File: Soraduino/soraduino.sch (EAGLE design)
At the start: 21 parts, among them IC1 ATMEGA168-AU, IC2 317EMP, IC3 317EMP

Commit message: 仮配線完了
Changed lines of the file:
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@@
 <wire x1="172.72" y1="0" x2="162.56" y2="0" width="0.1524" layer="91"/>
 <junction x="162.56" y="0"/>
-<junction x="172.72" y="0"/>
 <pinref part="IC4" gate="G$1" pin="DCPROG"/>
 <wire x1="137.16" y1="86.36" x2="162.56" y2="86.36" width="0.1524" layer="91"/>
 <junction x="162.56" y="86.36"/>
-<wire x1="172.72" y1="0" x2="254" y2="0" width="0.1524" layer="91"/>
 <pinref part="JAIRO-ANA" gate="G$1" pin="2"/>
 </segment>
@@
 </sheet>
 </sheets>
+<errors>
+</errors>
 </schematic>
 </drawing>

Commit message: back GPS 1
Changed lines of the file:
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@@
 <wire x1="172.72" y1="0" x2="162.56" y2="0" width="0.1524" layer="91"/>
 <junction x="162.56" y="0"/>
+<junction x="172.72" y="0"/>
 <pinref part="IC4" gate="G$1" pin="DCPROG"/>
 <wire x1="137.16" y1="86.36" x2="162.56" y2="86.36" width="0.1524" layer="91"/>
 <junction x="162.56" y="86.36"/>
+<wire x1="172.72" y1="0" x2="254" y2="0" width="0.1524" layer="91"/>
 <pinref part="JAIRO-ANA" gate="G$1" pin="2"/>
 </segment>
@@
 </sheet>
 </sheets>
-<errors>
-</errors>
 </schematic>
 </drawing>

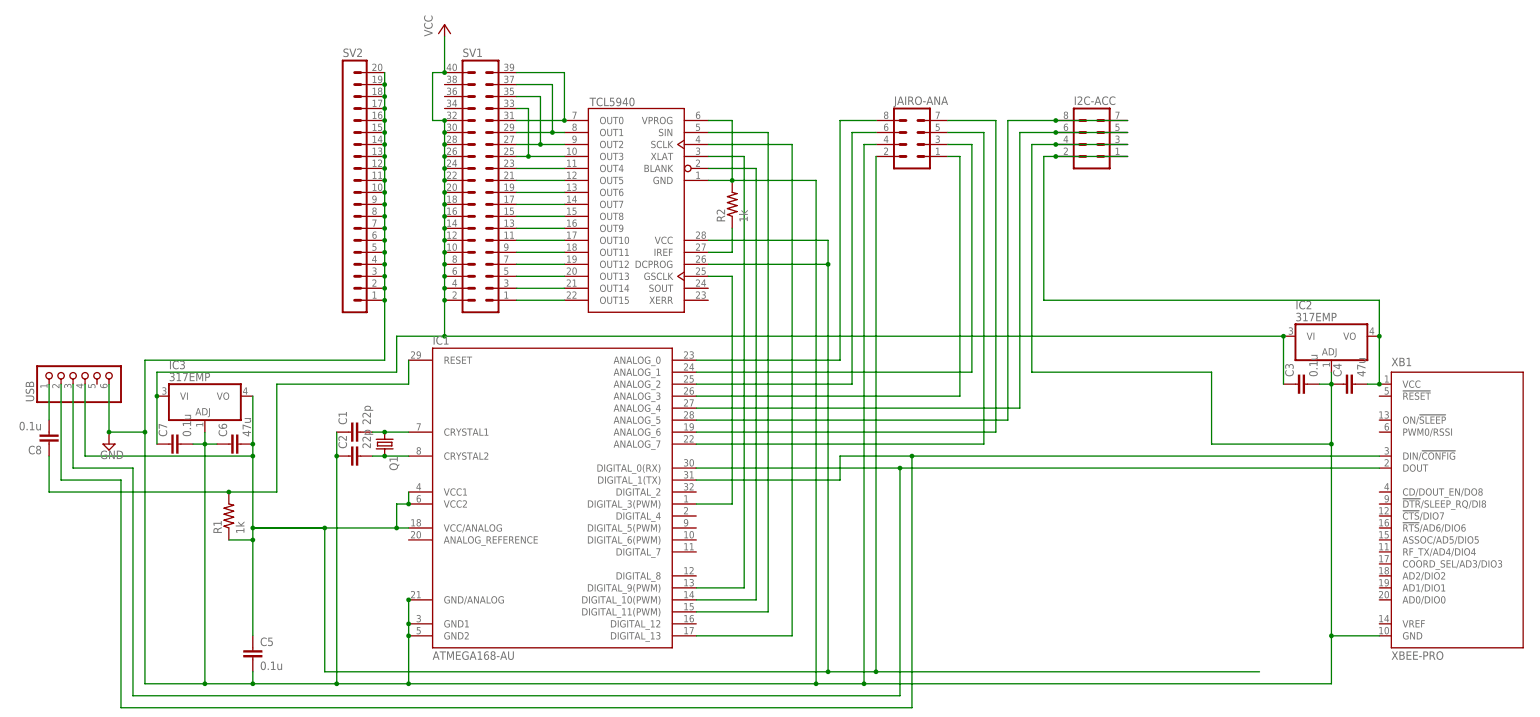
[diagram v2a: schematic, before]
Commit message: Revert "GPS、Digital出力を一旦削除"
This reverts commit f31cc228a309c3dd5619f128104a36497abb7aed.
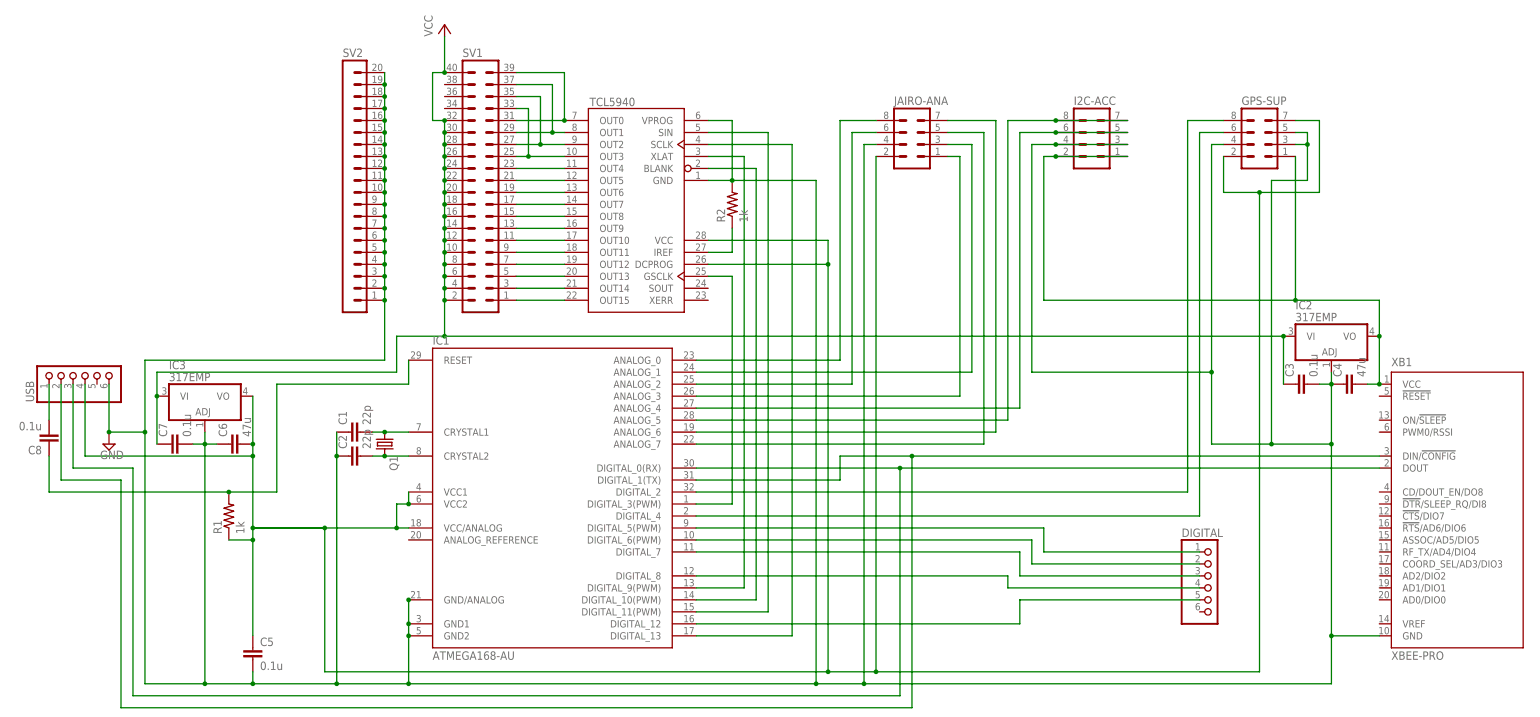
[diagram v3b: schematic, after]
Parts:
- added DIGITAL: (no value), pinhead:PINHD-1X6
- added GPS-SUP: (no value), con-lstb:MA04-2
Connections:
- new net N$36: GPS-SUP.8, IC1.DIGITAL_2
- new net N$37: GPS-SUP.6, IC1.DIGITAL_4
- new net N$39: DIGITAL.1, IC1.DIGITAL_5(PWM)
- new net N$40: DIGITAL.2, IC1.DIGITAL_6(PWM)
- new net N$41: DIGITAL.3, IC1.DIGITAL_7
- new net N$42: DIGITAL.4, IC1.DIGITAL_8
- new net N$47: DIGITAL.5, IC1.DIGITAL_12
- net GND: now also GPS-SUP.3, GPS-SUP.4, GPS-SUP.5
- net N$6: now also GPS-SUP.1
- net N$7: now also GPS-SUP.2, GPS-SUP.7
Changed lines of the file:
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@@
 <part name="R1" library="rcl" deviceset="R-US_" device="R0603" value="1k"/>
 <part name="R2" library="rcl" deviceset="R-US_" device="R0603" value="1k"/>
+<part name="DIGITAL" library="pinhead" deviceset="PINHD-1X6" device=""/>
 <part name="SV1" library="con-lstb" deviceset="MA20-2" device=""/>
 <part name="SV2" library="con-lstb" deviceset="MA20-1" device=""/>
 <part name="JAIRO-ANA" library="con-lstb" deviceset="MA04-2" device=""/>
 <part name="I2C-ACC" library="con-lstb" deviceset="MA04-2" device=""/>
+<part name="GPS-SUP" library="con-lstb" deviceset="MA04-2" device=""/>
 <part name="SUPPLY1" library="supply2" deviceset="GND" device=""/>
 <part name="P+1" library="supply1" deviceset="VCC" device=""/>
@@
 <instance part="R1" gate="G$1" x="35.56" y="33.02" rot="R90"/>
 <instance part="R2" gate="G$1" x="142.24" y="99.06" rot="R90"/>
+<instance part="DIGITAL" gate="A" x="243.84" y="17.78"/>
 <instance part="SV1" gate="G$1" x="88.9" y="104.14"/>
 <instance part="SV2" gate="1" x="60.96" y="101.6"/>
 <instance part="JAIRO-ANA" gate="G$1" x="180.34" y="114.3"/>
 <instance part="I2C-ACC" gate="G$1" x="218.44" y="114.3"/>
+<instance part="GPS-SUP" gate="G$1" x="254" y="114.3"/>
 <instance part="SUPPLY1" gate="GND" x="10.16" y="48.26"/>
 <instance part="P+1" gate="VCC" x="81.28" y="137.16"/>
@@
 <pinref part="C4" gate="G$1" pin="2"/>
 <junction x="279.4" y="60.96"/>
-<wire x1="208.28" y1="78.74" x2="279.4" y2="78.74" width="0.1524" layer="91"/>
+<wire x1="208.28" y1="78.74" x2="261.62" y2="78.74" width="0.1524" layer="91"/>
+<wire x1="261.62" y1="78.74" x2="279.4" y2="78.74" width="0.1524" layer="91"/>
 <wire x1="279.4" y1="78.74" x2="279.4" y2="71.12" width="0.1524" layer="91"/>
 <junction x="279.4" y="71.12"/>
@@
 <wire x1="208.28" y1="78.74" x2="208.28" y2="109.22" width="0.1524" layer="91"/>
 <wire x1="208.28" y1="109.22" x2="210.82" y2="109.22" width="0.1524" layer="91"/>
+<pinref part="GPS-SUP" gate="G$1" pin="1"/>
+<wire x1="261.62" y1="109.22" x2="261.62" y2="78.74" width="0.1524" layer="91"/>
+<junction x="261.62" y="78.74"/>
 <pinref part="I2C-ACC" gate="G$1" pin="1"/>
 <wire x1="210.82" y1="109.22" x2="226.06" y2="109.22" width="0.1524" layer="91"/>
@@
 </segment>
 </net>
+<net name="N$36" class="0">
+<segment>
+<pinref part="IC1" gate="1" pin="DIGITAL_2"/>
+<wire x1="134.62" y1="38.1" x2="238.76" y2="38.1" width="0.1524" layer="91"/>
+<wire x1="238.76" y1="38.1" x2="238.76" y2="116.84" width="0.1524" layer="91"/>
+<pinref part="GPS-SUP" gate="G$1" pin="8"/>
+<wire x1="238.76" y1="116.84" x2="246.38" y2="116.84" width="0.1524" layer="91"/>
+</segment>
+</net>
+<net name="N$37" class="0">
+<segment>
+<pinref part="IC1" gate="1" pin="DIGITAL_4"/>
+<wire x1="134.62" y1="33.02" x2="241.3" y2="33.02" width="0.1524" layer="91"/>
+<wire x1="241.3" y1="33.02" x2="241.3" y2="114.3" width="0.1524" layer="91"/>
+<pinref part="GPS-SUP" gate="G$1" pin="6"/>
+<wire x1="241.3" y1="114.3" x2="246.38" y2="114.3" width="0.1524" layer="91"/>
+</segment>
+</net>
 <net name="N$38" class="0">
 <segment>
@@
 <wire x1="137.16" y1="88.9" x2="142.24" y2="88.9" width="0.1524" layer="91"/>
 <wire x1="142.24" y1="88.9" x2="142.24" y2="93.98" width="0.1524" layer="91"/>
+</segment>
+</net>
+<net name="N$39" class="0">
+<segment>
+<pinref part="IC1" gate="1" pin="DIGITAL_5(PWM)"/>
+<wire x1="134.62" y1="30.48" x2="208.28" y2="30.48" width="0.1524" layer="91"/>
+<pinref part="DIGITAL" gate="A" pin="1"/>
+<wire x1="208.28" y1="30.48" x2="208.28" y2="25.4" width="0.1524" layer="91"/>
+<wire x1="208.28" y1="25.4" x2="241.3" y2="25.4" width="0.1524" layer="91"/>
+</segment>
+</net>
+<net name="N$40" class="0">
+<segment>
+<pinref part="IC1" gate="1" pin="DIGITAL_6(PWM)"/>
+<wire x1="134.62" y1="27.94" x2="205.74" y2="27.94" width="0.1524" layer="91"/>
+<pinref part="DIGITAL" gate="A" pin="2"/>
+<wire x1="205.74" y1="27.94" x2="205.74" y2="22.86" width="0.1524" layer="91"/>
+<wire x1="205.74" y1="22.86" x2="241.3" y2="22.86" width="0.1524" layer="91"/>
+</segment>
+</net>
+<net name="N$41" class="0">
+<segment>
+<pinref part="IC1" gate="1" pin="DIGITAL_7"/>
+<wire x1="134.62" y1="25.4" x2="203.2" y2="25.4" width="0.1524" layer="91"/>
+<pinref part="DIGITAL" gate="A" pin="3"/>
+<wire x1="203.2" y1="25.4" x2="203.2" y2="20.32" width="0.1524" layer="91"/>
+<wire x1="203.2" y1="20.32" x2="241.3" y2="20.32" width="0.1524" layer="91"/>
+</segment>
+</net>
+<net name="N$42" class="0">
+<segment>
+<pinref part="IC1" gate="1" pin="DIGITAL_8"/>
+<wire x1="134.62" y1="20.32" x2="200.66" y2="20.32" width="0.1524" layer="91"/>
+<pinref part="DIGITAL" gate="A" pin="4"/>
+<wire x1="200.66" y1="20.32" x2="200.66" y2="17.78" width="0.1524" layer="91"/>
+<wire x1="200.66" y1="17.78" x2="241.3" y2="17.78" width="0.1524" layer="91"/>
+</segment>
+</net>
+<net name="N$47" class="0">
+<segment>
+<pinref part="IC1" gate="1" pin="DIGITAL_12"/>
+<wire x1="134.62" y1="10.16" x2="203.2" y2="10.16" width="0.1524" layer="91"/>
+<pinref part="DIGITAL" gate="A" pin="5"/>
+<wire x1="203.2" y1="10.16" x2="203.2" y2="15.24" width="0.1524" layer="91"/>
+<wire x1="203.2" y1="15.24" x2="241.3" y2="15.24" width="0.1524" layer="91"/>
 </segment>
 </net>
@@
 <net name="N$7" class="0">
 <segment>
+<pinref part="GPS-SUP" gate="G$1" pin="7"/>
+<wire x1="261.62" y1="116.84" x2="266.7" y2="116.84" width="0.1524" layer="91"/>
+<wire x1="266.7" y1="116.84" x2="266.7" y2="101.6" width="0.1524" layer="91"/>
+<wire x1="266.7" y1="101.6" x2="254" y2="101.6" width="0.1524" layer="91"/>
 <pinref part="IC3" gate="A1" pin="VO"/>
 <pinref part="C6" gate="G$1" pin="2"/>
@@
 <wire x1="172.72" y1="0" x2="254" y2="0" width="0.1524" layer="91"/>
 <pinref part="JAIRO-ANA" gate="G$1" pin="2"/>
+<wire x1="254" y1="101.6" x2="254" y2="0" width="0.1524" layer="91"/>
+<pinref part="GPS-SUP" gate="G$1" pin="2"/>
+<wire x1="246.38" y1="109.22" x2="246.38" y2="101.6" width="0.1524" layer="91"/>
+<wire x1="246.38" y1="101.6" x2="254" y2="101.6" width="0.1524" layer="91"/>
+<junction x="254" y="101.6"/>
 </segment>
 </net>
@@
 <net name="GND" class="0">
 <segment>
+<pinref part="GPS-SUP" gate="G$1" pin="4"/>
+<wire x1="246.38" y1="111.76" x2="243.84" y2="111.76" width="0.1524" layer="91"/>
+<wire x1="243.84" y1="111.76" x2="243.84" y2="63.5" width="0.1524" layer="91"/>
 <wire x1="205.74" y1="111.76" x2="210.82" y2="111.76" width="0.1524" layer="91"/>
 <wire x1="205.74" y1="111.76" x2="205.74" y2="63.5" width="0.1524" layer="91"/>
@@
 <wire x1="170.18" y1="111.76" x2="172.72" y2="111.76" width="0.1524" layer="91"/>
 <wire x1="243.84" y1="63.5" x2="243.84" y2="48.26" width="0.1524" layer="91"/>
+<wire x1="243.84" y1="48.26" x2="256.54" y2="48.26" width="0.1524" layer="91"/>
+<junction x="243.84" y="63.5"/>
 <junction x="269.24" y="48.26"/>
-<wire x1="243.84" y1="48.26" x2="269.24" y2="48.26" width="0.1524" layer="91"/>
+<wire x1="256.54" y1="48.26" x2="269.24" y2="48.26" width="0.1524" layer="91"/>
+<wire x1="256.54" y1="48.26" x2="256.54" y2="104.14" width="0.1524" layer="91"/>
+<wire x1="256.54" y1="104.14" x2="264.16" y2="104.14" width="0.1524" layer="91"/>
+<pinref part="GPS-SUP" gate="G$1" pin="3"/>
+<wire x1="264.16" y1="104.14" x2="264.16" y2="111.76" width="0.1524" layer="91"/>
+<wire x1="264.16" y1="111.76" x2="261.62" y2="111.76" width="0.1524" layer="91"/>
+<junction x="256.54" y="48.26"/>
+<pinref part="GPS-SUP" gate="G$1" pin="5"/>
+<wire x1="264.16" y1="111.76" x2="264.16" y2="114.3" width="0.1524" layer="91"/>
+<wire x1="264.16" y1="114.3" x2="261.62" y2="114.3" width="0.1524" layer="91"/>
+<junction x="264.16" y="111.76"/>
 <pinref part="I2C-ACC" gate="G$1" pin="3"/>
 <wire x1="210.82" y1="111.76" x2="226.06" y2="111.76" width="0.1524" layer="91"/>
